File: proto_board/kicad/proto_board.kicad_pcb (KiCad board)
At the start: 2 copper layers, 80 x 50 mm, 1 part, among them J1 pcie_98

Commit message: Work in progress. Backlane kicad.
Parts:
- added H1: Bracket Hole, MountingHole:MountingHole_3.2mm_M3_Pad_Via, F.Cu at (95.5, 56.5)
- added H2: Bracket Hole, MountingHole:MountingHole_3.2mm_M3_Pad_Via, F.Cu at (95.4, 94.8)
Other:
- outline, holes or cut-outs redrawn

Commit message: Proto board work in progress.
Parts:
- removed H1, H2: Bracket Hole, MountingHole:MountingHole_3.2mm_M3_Pad_Via
- added J2: Conn_02x25_Odd_Even, Connector_PinHeader_2.00mm:PinHeader_2x25_P2.00mm_Vertical_SMD, F.Cu at (126.0, 96.1)
- added J3: Conn_02x25_Odd_Even, Connector_PinHeader_2.00mm:PinHeader_2x25_P2.00mm_Vertical_SMD, F.Cu at (126.0, 87.1)
- added TP1: TestPoint, proto_board:pad, F.Cu at (147.3, 55.9)
- added TP1: TestPoint, proto_board:pad, F.Cu at (144.8, 55.9)
- added TP1: TestPoint, proto_board:pad, F.Cu at (162.6, 86.4)
- added TP1: TestPoint, proto_board:pad, F.Cu at (149.9, 78.7)
- added TP1: TestPoint, proto_board:pad, F.Cu at (94.0, 58.4)
- added TP1: TestPoint, proto_board:pad, F.Cu at (129.5, 53.3)
- added TP1: TestPoint, proto_board:pad, F.Cu at (175.3, 86.4)
- added TP1: TestPoint, proto_board:pad, F.Cu at (157.5, 83.8)
- added TP1: TestPoint, proto_board:pad, F.Cu at (177.8, 43.2)
- added TP1: TestPoint, proto_board:pad, F.Cu at (170.2, 78.7)
- added TP1: TestPoint, proto_board:pad, F.Cu at (144.8, 81.3)
- added TP1: TestPoint, proto_board:pad, F.Cu at (142.2, 50.8)
- added TP1: TestPoint, proto_board:pad, F.Cu at (190.5, 43.2)
- added TP1: TestPoint, proto_board:pad, F.Cu at (127.0, 43.2)
- added TP1: TestPoint, proto_board:pad, F.Cu at (134.6, 50.8)
- added TP1: TestPoint, proto_board:pad, F.Cu at (114.3, 73.7)
- added TP1: TestPoint, proto_board:pad, F.Cu at (167.6, 66.0)
- added TP1: TestPoint, proto_board:pad, F.Cu at (180.3, 53.3)
- added TP1: TestPoint, proto_board:pad, F.Cu at (94.0, 76.2)
- added TP1: TestPoint, proto_board:pad, F.Cu at (175.3, 81.3)
- added TP1: TestPoint, proto_board:pad, F.Cu at (165.1, 91.4)
- added TP1: TestPoint, proto_board:pad, F.Cu at (101.6, 71.1)
- added TP1: TestPoint, proto_board:pad, F.Cu at (185.4, 81.3)
- added TP1: TestPoint, proto_board:pad, F.Cu at (101.6, 73.7)
- added TP1: TestPoint, proto_board:pad, F.Cu at (188.0, 81.3)
- added TP1: TestPoint, proto_board:pad, F.Cu at (180.3, 83.8)
- added TP1: TestPoint, proto_board:pad, F.Cu at (165.1, 81.3)
- added TP1: TestPoint, proto_board:pad, F.Cu at (188.0, 73.7)
- added TP1: TestPoint, proto_board:pad, F.Cu at (195.6, 83.8)
- added TP1: TestPoint, proto_board:pad, F.Cu at (111.8, 78.7)
- added TP1: TestPoint, proto_board:pad, F.Cu at (127.0, 73.7)
- added TP1: TestPoint, proto_board:pad, F.Cu at (139.7, 61.0)
- added TP1: TestPoint, proto_board:pad, F.Cu at (185.4, 61.0)
- added TP1: TestPoint, proto_board:pad, F.Cu at (180.3, 81.3)
- added TP1: TestPoint, proto_board:pad, F.Cu at (101.6, 76.2)
- added TP1: TestPoint, proto_board:pad, F.Cu at (170.2, 61.0)
- added TP1: TestPoint, proto_board:pad, F.Cu at (101.6, 43.2)
- added TP1: TestPoint, proto_board:pad, F.Cu at (144.8, 66.0)
- added TP1: TestPoint, proto_board:pad, F.Cu at (175.3, 45.7)
- added TP1: TestPoint, proto_board:pad, F.Cu at (96.5, 88.9)
- added TP1: TestPoint, proto_board:pad, F.Cu at (152.4, 68.6)
- added TP1: TestPoint, proto_board:pad, F.Cu at (180.3, 91.4)
- added TP1: TestPoint, proto_board:pad, F.Cu at (91.4, 68.6)
- added TP1: TestPoint, proto_board:pad, F.Cu at (134.6, 48.3)
- added TP1: TestPoint, proto_board:pad, F.Cu at (170.2, 68.6)
- added TP1: TestPoint, proto_board:pad, F.Cu at (142.2, 55.9)
- added TP1: TestPoint, proto_board:pad, F.Cu at (167.6, 96.5)
- added TP1: TestPoint, proto_board:pad, F.Cu at (94.0, 63.5)
- added TP1: TestPoint, proto_board:pad, F.Cu at (96.5, 53.3)
- added TP1: TestPoint, proto_board:pad, F.Cu at (144.8, 48.3)
- added TP1: TestPoint, proto_board:pad, F.Cu at (124.5, 50.8)
- added TP1: TestPoint, proto_board:pad, F.Cu at (111.8, 43.2)
- added TP1: TestPoint, proto_board:pad, F.Cu at (91.4, 61.0)
- added TP1: TestPoint, proto_board:pad, F.Cu at (149.9, 48.3)
- added TP1: TestPoint, proto_board:pad, F.Cu at (106.7, 50.8)
- added TP1: TestPoint, proto_board:pad, F.Cu at (132.1, 76.2)
- added TP1: TestPoint, proto_board:pad, F.Cu at (114.3, 71.1)
- added TP1: TestPoint, proto_board:pad, F.Cu at (177.8, 76.2)
- added TP1: TestPoint, proto_board:pad, F.Cu at (94.0, 68.6)
- added TP1: TestPoint, proto_board:pad, F.Cu at (137.2, 66.0)
- added TP1: TestPoint, proto_board:pad, F.Cu at (195.6, 86.4)
- added TP1: TestPoint, proto_board:pad, F.Cu at (185.4, 78.7)
- added TP1: TestPoint, proto_board:pad, F.Cu at (152.4, 55.9)
- added TP1: TestPoint, proto_board:pad, F.Cu at (193.0, 48.3)
- added TP1: TestPoint, proto_board:pad, F.Cu at (198.1, 73.7)
- added TP1: TestPoint, proto_board:pad, F.Cu at (160.0, 96.5)
- added TP1: TestPoint, proto_board:pad, F.Cu at (129.5, 68.6)
- added TP1: TestPoint, proto_board:pad, F.Cu at (180.3, 58.4)
- added TP1: TestPoint, proto_board:pad, F.Cu at (190.5, 96.5)
- added TP1: TestPoint, proto_board:pad, F.Cu at (121.9, 50.8)
- added TP1: TestPoint, proto_board:pad, F.Cu at (142.2, 43.2)
- added TP1: TestPoint, proto_board:pad, F.Cu at (132.1, 50.8)
- added TP1: TestPoint, proto_board:pad, F.Cu at (182.9, 58.4)
- added TP1: TestPoint, proto_board:pad, F.Cu at (195.6, 96.5)
- added TP1: TestPoint, proto_board:pad, F.Cu at (177.8, 58.4)
- added TP1: TestPoint, proto_board:pad, F.Cu at (99.1, 73.7)
- added TP1: TestPoint, proto_board:pad, F.Cu at (167.6, 45.7)
- added TP1: TestPoint, proto_board:pad, F.Cu at (190.5, 55.9)
- added TP1: TestPoint, proto_board:pad, F.Cu at (137.2, 71.1)
- added TP1: TestPoint, proto_board:pad, F.Cu at (147.3, 58.4)
- added TP1: TestPoint, proto_board:pad, F.Cu at (177.8, 83.8)
- added TP1: TestPoint, proto_board:pad, F.Cu at (139.7, 55.9)
- added TP1: TestPoint, proto_board:pad, F.Cu at (165.1, 66.0)
- added TP1: TestPoint, proto_board:pad, F.Cu at (154.9, 96.5)
- added TP1: TestPoint, proto_board:pad, F.Cu at (172.7, 94.0)
- added TP1: TestPoint, proto_board:pad, F.Cu at (152.4, 50.8)
- added TP1: TestPoint, proto_board:pad, F.Cu at (127.0, 53.3)
- added TP1: TestPoint, proto_board:pad, F.Cu at (139.7, 76.2)
- added TP1: TestPoint, proto_board:pad, F.Cu at (96.5, 50.8)
- added TP1: TestPoint, proto_board:pad, F.Cu at (195.6, 94.0)
- added TP1: TestPoint, proto_board:pad, F.Cu at (106.7, 66.0)
- added TP1: TestPoint, proto_board:pad, F.Cu at (198.1, 63.5)
- added TP1: TestPoint, proto_board:pad, F.Cu at (99.1, 58.4)
- added TP1: TestPoint, proto_board:pad, F.Cu at (99.1, 76.2)
- added TP1: TestPoint, proto_board:pad, F.Cu at (106.7, 61.0)
- added TP1: TestPoint, proto_board:pad, F.Cu at (167.6, 76.2)
- added TP1: TestPoint, proto_board:pad, F.Cu at (91.4, 50.8)
- added TP1: TestPoint, proto_board:pad, F.Cu at (185.4, 71.1)
- added TP1: TestPoint, proto_board:pad, F.Cu at (193.0, 96.5)
- added TP1: TestPoint, proto_board:pad, F.Cu at (193.0, 94.0)
- added TP1: TestPoint, proto_board:pad, F.Cu at (129.5, 61.0)
- added TP1: TestPoint, proto_board:pad, F.Cu at (124.5, 71.1)
- added TP1: TestPoint, proto_board:pad, F.Cu at (129.5, 58.4)
- added TP1: TestPoint, proto_board:pad, F.Cu at (144.8, 76.2)
- added TP1: TestPoint, proto_board:pad, F.Cu at (96.5, 58.4)
- added TP1: TestPoint, proto_board:pad, F.Cu at (188.0, 45.7)
- added TP1: TestPoint, proto_board:pad, F.Cu at (139.7, 50.8)
- added TP1: TestPoint, proto_board:pad, F.Cu at (114.3, 61.0)
- added TP1: TestPoint, proto_board:pad, F.Cu at (188.0, 96.5)
- added TP1: TestPoint, proto_board:pad, F.Cu at (198.1, 43.2)
- added TP1: TestPoint, proto_board:pad, F.Cu at (185.4, 53.3)
- added TP1: TestPoint, proto_board:pad, F.Cu at (96.5, 63.5)
- added TP1: TestPoint, proto_board:pad, F.Cu at (195.6, 68.6)
- added TP1: TestPoint, proto_board:pad, F.Cu at (182.9, 96.5)
- added TP1: TestPoint, proto_board:pad, F.Cu at (180.3, 61.0)
- added TP1: TestPoint, proto_board:pad, F.Cu at (129.5, 48.3)
- added TP1: TestPoint, proto_board:pad, F.Cu at (160.0, 94.0)
- added TP1: TestPoint, proto_board:pad, F.Cu at (188.0, 68.6)
- added TP1: TestPoint, proto_board:pad, F.Cu at (170.2, 55.9)
- added TP1: TestPoint, proto_board:pad, F.Cu at (185.4, 91.4)
- added TP1: TestPoint, proto_board:pad, F.Cu at (180.3, 86.4)
- added TP1: TestPoint, proto_board:pad, F.Cu at (160.0, 61.0)
- added TP1: TestPoint, proto_board:pad, F.Cu at (185.4, 63.5)
- added TP1: TestPoint, proto_board:pad, F.Cu at (195.6, 55.9)
- added TP1: TestPoint, proto_board:pad, F.Cu at (182.9, 83.8)
- added TP1: TestPoint, proto_board:pad, F.Cu at (162.6, 76.2)
- added TP1: TestPoint, proto_board:pad, F.Cu at (154.9, 91.4)
- added TP1: TestPoint, proto_board:pad, F.Cu at (154.9, 45.7)
- added TP1: TestPoint, proto_board:pad, F.Cu at (162.6, 58.4)
- added TP1: TestPoint, proto_board:pad, F.Cu at (147.3, 53.3)
- added TP1: TestPoint, proto_board:pad, F.Cu at (124.5, 66.0)
- added TP1: TestPoint, proto_board:pad, F.Cu at (149.9, 76.2)
- added TP1: TestPoint, proto_board:pad, F.Cu at (170.2, 96.5)
- added TP1: TestPoint, proto_board:pad, F.Cu at (172.7, 50.8)
- added TP1: TestPoint, proto_board:pad, F.Cu at (94.0, 48.3)
- added TP1: TestPoint, proto_board:pad, F.Cu at (177.8, 86.4)
- added TP1: TestPoint, proto_board:pad, F.Cu at (149.9, 66.0)
- added TP1: TestPoint, proto_board:pad, F.Cu at (127.0, 58.4)
- added TP1: TestPoint, proto_board:pad, F.Cu at (119.4, 50.8)
- added TP1: TestPoint, proto_board:pad, F.Cu at (124.5, 45.7)
- added TP1: TestPoint, proto_board:pad, F.Cu at (190.5, 68.6)
- added TP1: TestPoint, proto_board:pad, F.Cu at (137.2, 73.7)
- added TP1: TestPoint, proto_board:pad, F.Cu at (193.0, 86.4)
- added TP1: TestPoint, proto_board:pad, F.Cu at (157.5, 53.3)
- added TP1: TestPoint, proto_board:pad, F.Cu at (165.1, 68.6)
- added TP1: TestPoint, proto_board:pad, F.Cu at (167.6, 81.3)
- added TP1: TestPoint, proto_board:pad, F.Cu at (198.1, 91.4)
- added TP1: TestPoint, proto_board:pad, F.Cu at (162.6, 50.8)
- added TP1: TestPoint, proto_board:pad, F.Cu at (147.3, 63.5)
- added TP1: TestPoint, proto_board:pad, F.Cu at (198.1, 88.9)
- added TP1: TestPoint, proto_board:pad, F.Cu at (154.9, 73.7)
- added TP1: TestPoint, proto_board:pad, F.Cu at (182.9, 55.9)
- added TP1: TestPoint, proto_board:pad, F.Cu at (162.6, 91.4)
- added TP1: TestPoint, proto_board:pad, F.Cu at (109.2, 71.1)
- added TP1: TestPoint, proto_board:pad, F.Cu at (167.6, 94.0)
- added TP1: TestPoint, proto_board:pad, F.Cu at (188.0, 66.0)
- added TP1: TestPoint, proto_board:pad, F.Cu at (129.5, 81.3)
- added TP1: TestPoint, proto_board:pad, F.Cu at (109.2, 50.8)
- added TP1: TestPoint, proto_board:pad, F.Cu at (198.1, 61.0)
- added TP1: TestPoint, proto_board:pad, F.Cu at (182.9, 78.7)
- added TP1: TestPoint, proto_board:pad, F.Cu at (144.8, 50.8)
- added TP1: TestPoint, proto_board:pad, F.Cu at (147.3, 50.8)
- added TP1: TestPoint, proto_board:pad, F.Cu at (104.1, 68.6)
- added TP1: TestPoint, proto_board:pad, F.Cu at (195.6, 53.3)
- added TP1: TestPoint, proto_board:pad, F.Cu at (101.6, 63.5)
- added TP1: TestPoint, proto_board:pad, F.Cu at (111.8, 48.3)
- added TP1: TestPoint, proto_board:pad, F.Cu at (167.6, 63.5)
- added TP1: TestPoint, proto_board:pad, F.Cu at (142.2, 53.3)
- added TP1: TestPoint, proto_board:pad, F.Cu at (134.6, 45.7)
- added TP1: TestPoint, proto_board:pad, F.Cu at (109.2, 63.5)
- added TP1: TestPoint, proto_board:pad, F.Cu at (124.5, 81.3)
- added TP1: TestPoint, proto_board:pad, F.Cu at (162.6, 81.3)
- added TP1: TestPoint, proto_board:pad, F.Cu at (134.6, 81.3)
- added TP1: TestPoint, proto_board:pad, F.Cu at (137.2, 58.4)
- added TP1: TestPoint, proto_board:pad, F.Cu at (154.9, 88.9)
- added TP1: TestPoint, proto_board:pad, F.Cu at (152.4, 48.3)
- added TP1: TestPoint, proto_board:pad, F.Cu at (172.7, 96.5)
- added TP1: TestPoint, proto_board:pad, F.Cu at (94.0, 83.8)
- added TP1: TestPoint, proto_board:pad, F.Cu at (175.3, 55.9)
- added TP1: TestPoint, proto_board:pad, F.Cu at (119.4, 55.9)
- added TP1: TestPoint, proto_board:pad, F.Cu at (162.6, 66.0)
- added TP1: TestPoint, proto_board:pad, F.Cu at (142.2, 73.7)
- added TP1: TestPoint, proto_board:pad, F.Cu at (198.1, 96.5)
- added TP1: TestPoint, proto_board:pad, F.Cu at (152.4, 45.7)
- added TP1: TestPoint, proto_board:pad, F.Cu at (121.9, 55.9)
- added TP1: TestPoint, proto_board:pad, F.Cu at (195.6, 63.5)
- added TP1: TestPoint, proto_board:pad, F.Cu at (111.8, 71.1)
- added TP1: TestPoint, proto_board:pad, F.Cu at (157.5, 94.0)
- added TP1: TestPoint, proto_board:pad, F.Cu at (188.0, 71.1)
- added TP1: TestPoint, proto_board:pad, F.Cu at (170.2, 88.9)
- added TP1: TestPoint, proto_board:pad, F.Cu at (119.4, 43.2)
- added TP1: TestPoint, proto_board:pad, F.Cu at (111.8, 61.0)
- added TP1: TestPoint, proto_board:pad, F.Cu at (147.3, 78.7)
- added TP1: TestPoint, proto_board:pad, F.Cu at (154.9, 66.0)
- added TP1: TestPoint, proto_board:pad, F.Cu at (106.7, 78.7)
- added TP1: TestPoint, proto_board:pad, F.Cu at (172.7, 53.3)
- added TP1: TestPoint, proto_board:pad, F.Cu at (182.9, 76.2)
- added TP1: TestPoint, proto_board:pad, F.Cu at (147.3, 71.1)
- added TP1: TestPoint, proto_board:pad, F.Cu at (157.5, 76.2)
- added TP1: TestPoint, proto_board:pad, F.Cu at (109.2, 66.0)
- added TP1: TestPoint, proto_board:pad, F.Cu at (114.3, 58.4)
- added TP1: TestPoint, proto_board:pad, F.Cu at (185.4, 66.0)
- added TP1: TestPoint, proto_board:pad, F.Cu at (195.6, 66.0)
- added TP1: TestPoint, proto_board:pad, F.Cu at (99.1, 68.6)
- added TP1: TestPoint, proto_board:pad, F.Cu at (127.0, 55.9)
- added TP1: TestPoint, proto_board:pad, F.Cu at (121.9, 63.5)
- added TP1: TestPoint, proto_board:pad, F.Cu at (121.9, 78.7)
- added TP1: TestPoint, proto_board:pad, F.Cu at (144.8, 43.2)
- added TP1: TestPoint, proto_board:pad, F.Cu at (116.8, 78.7)
- added TP1: TestPoint, proto_board:pad, F.Cu at (119.4, 53.3)
- added TP1: TestPoint, proto_board:pad, F.Cu at (124.5, 58.4)
- added TP1: TestPoint, proto_board:pad, F.Cu at (149.9, 81.3)
- added TP1: TestPoint, proto_board:pad, F.Cu at (190.5, 88.9)
- added TP1: TestPoint, proto_board:pad, F.Cu at (175.3, 88.9)
- added TP1: TestPoint, proto_board:pad, F.Cu at (182.9, 50.8)
- added TP1: TestPoint, proto_board:pad, F.Cu at (111.8, 76.2)
- added TP1: TestPoint, proto_board:pad, F.Cu at (165.1, 73.7)
- added TP1: TestPoint, proto_board:pad, F.Cu at (96.5, 76.2)
- added TP1: TestPoint, proto_board:pad, F.Cu at (162.6, 78.7)
- added TP1: TestPoint, proto_board:pad, F.Cu at (147.3, 73.7)
- added TP1: TestPoint, proto_board:pad, F.Cu at (170.2, 86.4)
- added TP1: TestPoint, proto_board:pad, F.Cu at (121.9, 76.2)
- added TP1: TestPoint, proto_board:pad, F.Cu at (193.0, 81.3)
- added TP1: TestPoint, proto_board:pad, F.Cu at (142.2, 78.7)
- added TP1: TestPoint, proto_board:pad, F.Cu at (182.9, 94.0)
- added TP1: TestPoint, proto_board:pad, F.Cu at (91.4, 76.2)
- added TP1: TestPoint, proto_board:pad, F.Cu at (139.7, 53.3)
- added TP1: TestPoint, proto_board:pad, F.Cu at (188.0, 55.9)
- added TP1: TestPoint, proto_board:pad, F.Cu at (175.3, 76.2)
- added TP1: TestPoint, proto_board:pad, F.Cu at (193.0, 91.4)
- added TP1: TestPoint, proto_board:pad, F.Cu at (106.7, 45.7)
- added TP1: TestPoint, proto_board:pad, F.Cu at (170.2, 76.2)
- added TP1: TestPoint, proto_board:pad, F.Cu at (127.0, 81.3)
- added TP1: TestPoint, proto_board:pad, F.Cu at (188.0, 61.0)
- added TP1: TestPoint, proto_board:pad, F.Cu at (160.0, 76.2)
- added TP1: TestPoint, proto_board:pad, F.Cu at (109.2, 55.9)
- added TP1: TestPoint, proto_board:pad, F.Cu at (94.0, 50.8)
- added TP1: TestPoint, proto_board:pad, F.Cu at (111.8, 81.3)
- added TP1: TestPoint, proto_board:pad, F.Cu at (190.5, 58.4)
- added TP1: TestPoint, proto_board:pad, F.Cu at (116.8, 48.3)
- added TP1: TestPoint, proto_board:pad, F.Cu at (109.2, 48.3)
- added TP1: TestPoint, proto_board:pad, F.Cu at (152.4, 81.3)
- added TP1: TestPoint, proto_board:pad, F.Cu at (157.5, 73.7)
- added TP1: TestPoint, proto_board:pad, F.Cu at (195.6, 48.3)
- added TP1: TestPoint, proto_board:pad, F.Cu at (170.2, 58.4)
- added TP1: TestPoint, proto_board:pad, F.Cu at (165.1, 45.7)
- added TP1: TestPoint, proto_board:pad, F.Cu at (177.8, 45.7)
- added TP1: TestPoint, proto_board:pad, F.Cu at (137.2, 68.6)
- added TP1: TestPoint, proto_board:pad, F.Cu at (127.0, 78.7)
- added TP1: TestPoint, proto_board:pad, F.Cu at (129.5, 71.1)
- added TP1: TestPoint, proto_board:pad, F.Cu at (198.1, 81.3)
- added TP1: TestPoint, proto_board:pad, F.Cu at (175.3, 58.4)
- added TP1: TestPoint, proto_board:pad, F.Cu at (182.9, 81.3)
- added TP1: TestPoint, proto_board:pad, F.Cu at (170.2, 83.8)
- added TP1: TestPoint, proto_board:pad, F.Cu at (129.5, 55.9)
- added TP1: TestPoint, proto_board:pad, F.Cu at (165.1, 61.0)
- added TP1: TestPoint, proto_board:pad, F.Cu at (124.5, 43.2)
- added TP1: TestPoint, proto_board:pad, F.Cu at (139.7, 78.7)
- added TP1: TestPoint, proto_board:pad, F.Cu at (172.7, 68.6)
- added TP1: TestPoint, proto_board:pad, F.Cu at (172.7, 76.2)
- added TP1: TestPoint, proto_board:pad, F.Cu at (132.1, 48.3)
- added TP1: TestPoint, proto_board:pad, F.Cu at (127.0, 48.3)
- added TP1: TestPoint, proto_board:pad, F.Cu at (132.1, 66.0)
- added TP1: TestPoint, proto_board:pad, F.Cu at (157.5, 86.4)
- added TP1: TestPoint, proto_board:pad, F.Cu at (157.5, 48.3)
- added TP1: TestPoint, proto_board:pad, F.Cu at (175.3, 43.2)
- added TP1: TestPoint, proto_board:pad, F.Cu at (185.4, 50.8)
- added TP1: TestPoint, proto_board:pad, F.Cu at (96.5, 73.7)
- added TP1: TestPoint, proto_board:pad, F.Cu at (147.3, 61.0)
- added TP1: TestPoint, proto_board:pad, F.Cu at (116.8, 50.8)
- added TP1: TestPoint, proto_board:pad, F.Cu at (154.9, 53.3)
- added TP1: TestPoint, proto_board:pad, F.Cu at (154.9, 94.0)
- added TP1: TestPoint, proto_board:pad, F.Cu at (157.5, 55.9)
- added TP1: TestPoint, proto_board:pad, F.Cu at (116.8, 76.2)
- added TP1: TestPoint, proto_board:pad, F.Cu at (139.7, 66.0)
- added TP1: TestPoint, proto_board:pad, F.Cu at (142.2, 45.7)
- added TP1: TestPoint, proto_board:pad, F.Cu at (182.9, 43.2)
- added TP1: TestPoint, proto_board:pad, F.Cu at (96.5, 83.8)
- added TP1: TestPoint, proto_board:pad, F.Cu at (119.4, 81.3)
- added TP1: TestPoint, proto_board:pad, F.Cu at (94.0, 66.0)
- added TP1: TestPoint, proto_board:pad, F.Cu at (188.0, 63.5)
- added TP1: TestPoint, proto_board:pad, F.Cu at (111.8, 68.6)
- added TP1: TestPoint, proto_board:pad, F.Cu at (157.5, 91.4)
- added TP1: TestPoint, proto_board:pad, F.Cu at (175.3, 53.3)
- added TP1: TestPoint, proto_board:pad, F.Cu at (106.7, 53.3)
- added TP1: TestPoint, proto_board:pad, F.Cu at (119.4, 68.6)
- added TP1: TestPoint, proto_board:pad, F.Cu at (180.3, 88.9)
- added TP1: TestPoint, proto_board:pad, F.Cu at (142.2, 58.4)
- added TP1: TestPoint, proto_board:pad, F.Cu at (94.0, 78.7)
- added TP1: TestPoint, proto_board:pad, F.Cu at (157.5, 58.4)
- added TP1: TestPoint, proto_board:pad, F.Cu at (139.7, 43.2)
- added TP1: TestPoint, proto_board:pad, F.Cu at (182.9, 45.7)
- added TP1: TestPoint, proto_board:pad, F.Cu at (177.8, 91.4)
- added TP1: TestPoint, proto_board:pad, F.Cu at (152.4, 76.2)
- added TP1: TestPoint, proto_board:pad, F.Cu at (96.5, 61.0)
- added TP1: TestPoint, proto_board:pad, F.Cu at (180.3, 63.5)
- added TP1: TestPoint, proto_board:pad, F.Cu at (149.9, 61.0)
- added TP1: TestPoint, proto_board:pad, F.Cu at (195.6, 81.3)
- added TP1: TestPoint, proto_board:pad, F.Cu at (106.7, 63.5)
- added TP1: TestPoint, proto_board:pad, F.Cu at (137.2, 48.3)
- added TP1: TestPoint, proto_board:pad, F.Cu at (165.1, 76.2)
- added TP1: TestPoint, proto_board:pad, F.Cu at (91.4, 55.9)
- added TP1: TestPoint, proto_board:pad, F.Cu at (157.5, 71.1)
- added TP1: TestPoint, proto_board:pad, F.Cu at (137.2, 61.0)
- added TP1: TestPoint, proto_board:pad, F.Cu at (193.0, 53.3)
- added TP1: TestPoint, proto_board:pad, F.Cu at (190.5, 71.1)
- added TP1: TestPoint, proto_board:pad, F.Cu at (172.7, 61.0)
- added TP1: TestPoint, proto_board:pad, F.Cu at (157.5, 68.6)
- added TP1: TestPoint, proto_board:pad, F.Cu at (127.0, 63.5)
- added TP1: TestPoint, proto_board:pad, F.Cu at (119.4, 73.7)
- added TP1: TestPoint, proto_board:pad, F.Cu at (160.0, 68.6)
- added TP1: TestPoint, proto_board:pad, F.Cu at (160.0, 81.3)
- added TP1: TestPoint, proto_board:pad, F.Cu at (172.7, 43.2)
- added TP1: TestPoint, proto_board:pad, F.Cu at (94.0, 96.5)
- added TP1: TestPoint, proto_board:pad, F.Cu at (104.1, 45.7)
- added TP1: TestPoint, proto_board:pad, F.Cu at (152.4, 43.2)
- added TP1: TestPoint, proto_board:pad, F.Cu at (170.2, 43.2)
- added TP1: TestPoint, proto_board:pad, F.Cu at (190.5, 94.0)
- added TP1: TestPoint, proto_board:pad, F.Cu at (198.1, 68.6)
- added TP1: TestPoint, proto_board:pad, F.Cu at (195.6, 88.9)
- added TP1: TestPoint, proto_board:pad, F.Cu at (154.9, 81.3)
- added TP1: TestPoint, proto_board:pad, F.Cu at (99.1, 66.0)
- added TP1: TestPoint, proto_board:pad, F.Cu at (144.8, 45.7)
- added TP1: TestPoint, proto_board:pad, F.Cu at (157.5, 96.5)
- added TP1: TestPoint, proto_board:pad, F.Cu at (124.5, 48.3)
- added TP1: TestPoint, proto_board:pad, F.Cu at (101.6, 81.3)
- added TP1: TestPoint, proto_board:pad, F.Cu at (175.3, 50.8)
- added TP1: TestPoint, proto_board:pad, F.Cu at (139.7, 58.4)
- added TP1: TestPoint, proto_board:pad, F.Cu at (160.0, 66.0)
- added TP1: TestPoint, proto_board:pad, F.Cu at (157.5, 88.9)
- added TP1: TestPoint, proto_board:pad, F.Cu at (154.9, 83.8)
- added TP1: TestPoint, proto_board:pad, F.Cu at (147.3, 43.2)
- added TP1: TestPoint, proto_board:pad, F.Cu at (101.6, 58.4)
- added TP1: TestPoint, proto_board:pad, F.Cu at (139.7, 71.1)
- added TP1: TestPoint, proto_board:pad, F.Cu at (172.7, 71.1)
- added TP1: TestPoint, proto_board:pad, F.Cu at (160.0, 91.4)
- added TP1: TestPoint, proto_board:pad, F.Cu at (172.7, 45.7)
- added TP1: TestPoint, proto_board:pad, F.Cu at (137.2, 81.3)
- added TP1: TestPoint, proto_board:pad, F.Cu at (188.0, 76.2)
- added TP1: TestPoint, proto_board:pad, F.Cu at (170.2, 66.0)
- added TP1: TestPoint, proto_board:pad, F.Cu at (190.5, 81.3)
- added TP1: TestPoint, proto_board:pad, F.Cu at (182.9, 48.3)
- added TP1: TestPoint, proto_board:pad, F.Cu at (185.4, 73.7)
- added TP1: TestPoint, proto_board:pad, F.Cu at (137.2, 53.3)
- added TP1: TestPoint, proto_board:pad, F.Cu at (160.0, 73.7)
- added TP1: TestPoint, proto_board:pad, F.Cu at (172.7, 55.9)
- added TP1: TestPoint, proto_board:pad, F.Cu at (162.6, 83.8)
- added TP1: TestPoint, proto_board:pad, F.Cu at (104.1, 50.8)
- added TP1: TestPoint, proto_board:pad, F.Cu at (172.7, 63.5)
- added TP1: TestPoint, proto_board:pad, F.Cu at (121.9, 68.6)
- added TP1: TestPoint, proto_board:pad, F.Cu at (193.0, 66.0)
- added TP1: TestPoint, proto_board:pad, F.Cu at (175.3, 73.7)
- added TP1: TestPoint, proto_board:pad, F.Cu at (96.5, 94.0)
- added TP1: TestPoint, proto_board:pad, F.Cu at (91.4, 58.4)
- added TP1: TestPoint, proto_board:pad, F.Cu at (185.4, 76.2)
- added TP1: TestPoint, proto_board:pad, F.Cu at (185.4, 68.6)
- added TP1: TestPoint, proto_board:pad, F.Cu at (193.0, 58.4)
- added TP1: TestPoint, proto_board:pad, F.Cu at (147.3, 68.6)
- added TP1: TestPoint, proto_board:pad, F.Cu at (96.5, 78.7)
- added TP1: TestPoint, proto_board:pad, F.Cu at (170.2, 91.4)
- added TP1: TestPoint, proto_board:pad, F.Cu at (134.6, 63.5)
- added TP1: TestPoint, proto_board:pad, F.Cu at (134.6, 55.9)
- added TP1: TestPoint, proto_board:pad, F.Cu at (99.1, 53.3)
- added TP1: TestPoint, proto_board:pad, F.Cu at (124.5, 53.3)
- added TP1: TestPoint, proto_board:pad, F.Cu at (104.1, 81.3)
- added TP1: TestPoint, proto_board:pad, F.Cu at (193.0, 55.9)
- added TP1: TestPoint, proto_board:pad, F.Cu at (91.4, 78.7)
- added TP1: TestPoint, proto_board:pad, F.Cu at (172.7, 73.7)
- added TP1: TestPoint, proto_board:pad, F.Cu at (152.4, 73.7)
- added TP1: TestPoint, proto_board:pad, F.Cu at (193.0, 50.8)
- added TP1: TestPoint, proto_board:pad, F.Cu at (190.5, 48.3)
- added TP1: TestPoint, proto_board:pad, F.Cu at (182.9, 63.5)
- added TP1: TestPoint, proto_board:pad, F.Cu at (142.2, 48.3)
- added TP1: TestPoint, proto_board:pad, F.Cu at (172.7, 88.9)
- added TP1: TestPoint, proto_board:pad, F.Cu at (121.9, 45.7)
- added TP1: TestPoint, proto_board:pad, F.Cu at (137.2, 78.7)
- added TP1: TestPoint, proto_board:pad, F.Cu at (185.4, 96.5)
- added TP1: TestPoint, proto_board:pad, F.Cu at (195.6, 45.7)
- added TP1: TestPoint, proto_board:pad, F.Cu at (109.2, 76.2)
- added TP1: TestPoint, proto_board:pad, F.Cu at (142.2, 68.6)
- added TP1: TestPoint, proto_board:pad, F.Cu at (119.4, 58.4)
- added TP1: TestPoint, proto_board:pad, F.Cu at (137.2, 45.7)
- added TP1: TestPoint, proto_board:pad, F.Cu at (170.2, 73.7)
- added TP1: TestPoint, proto_board:pad, F.Cu at (91.4, 63.5)
- added TP1: TestPoint, proto_board:pad, F.Cu at (111.8, 73.7)
- added TP1: TestPoint, proto_board:pad, F.Cu at (109.2, 53.3)
- added TP1: TestPoint, proto_board:pad, F.Cu at (129.5, 50.8)
- added TP1: TestPoint, proto_board:pad, F.Cu at (165.1, 58.4)
- added TP1: TestPoint, proto_board:pad, F.Cu at (132.1, 78.7)
- added TP1: TestPoint, proto_board:pad, F.Cu at (160.0, 78.7)
- added TP1: TestPoint, proto_board:pad, F.Cu at (121.9, 71.1)
- added TP1: TestPoint, proto_board:pad, F.Cu at (139.7, 68.6)
- added TP1: TestPoint, proto_board:pad, F.Cu at (91.4, 48.3)
- added TP1: TestPoint, proto_board:pad, F.Cu at (101.6, 68.6)
- added TP1: TestPoint, proto_board:pad, F.Cu at (165.1, 83.8)
- added TP1: TestPoint, proto_board:pad, F.Cu at (175.3, 66.0)
- added TP1: TestPoint, proto_board:pad, F.Cu at (154.9, 71.1)
- added TP1: TestPoint, proto_board:pad, F.Cu at (188.0, 86.4)
- added TP1: TestPoint, proto_board:pad, F.Cu at (104.1, 61.0)
- added TP1: TestPoint, proto_board:pad, F.Cu at (185.4, 55.9)
- added TP1: TestPoint, proto_board:pad, F.Cu at (132.1, 45.7)
- added TP1: TestPoint, proto_board:pad, F.Cu at (111.8, 66.0)
- added TP1: TestPoint, proto_board:pad, F.Cu at (119.4, 76.2)
- added TP1: TestPoint, proto_board:pad, F.Cu at (99.1, 43.2)
- added TP1: TestPoint, proto_board:pad, F.Cu at (94.0, 45.7)
- added TP1: TestPoint, proto_board:pad, F.Cu at (144.8, 68.6)
- added TP1: TestPoint, proto_board:pad, F.Cu at (114.3, 50.8)
- added TP1: TestPoint, proto_board:pad, F.Cu at (94.0, 86.4)
- added TP1: TestPoint, proto_board:pad, F.Cu at (190.5, 50.8)
- added TP1: TestPoint, proto_board:pad, F.Cu at (193.0, 61.0)
- added TP1: TestPoint, proto_board:pad, F.Cu at (104.1, 53.3)
- added TP1: TestPoint, proto_board:pad, F.Cu at (195.6, 61.0)
- added TP1: TestPoint, proto_board:pad, F.Cu at (109.2, 73.7)
- added TP1: TestPoint, proto_board:pad, F.Cu at (127.0, 45.7)
- added TP1: TestPoint, proto_board:pad, F.Cu at (91.4, 96.5)
- added TP1: TestPoint, proto_board:pad, F.Cu at (142.2, 61.0)
- added TP1: TestPoint, proto_board:pad, F.Cu at (99.1, 78.7)
- added TP1: TestPoint, proto_board:pad, F.Cu at (91.4, 71.1)
- added TP1: TestPoint, proto_board:pad, F.Cu at (154.9, 55.9)
- added TP1: TestPoint, proto_board:pad, F.Cu at (180.3, 76.2)
- added TP1: TestPoint, proto_board:pad, F.Cu at (124.5, 61.0)
- added TP1: TestPoint, proto_board:pad, F.Cu at (139.7, 63.5)
- added TP1: TestPoint, proto_board:pad, F.Cu at (175.3, 48.3)
- added TP1: TestPoint, proto_board:pad, F.Cu at (180.3, 55.9)
- added TP1: TestPoint, proto_board:pad, F.Cu at (190.5, 86.4)
- added TP1: TestPoint, proto_board:pad, F.Cu at (195.6, 43.2)
- added TP1: TestPoint, proto_board:pad, F.Cu at (124.5, 73.7)
- added TP1: TestPoint, proto_board:pad, F.Cu at (91.4, 45.7)
- added TP1: TestPoint, proto_board:pad, F.Cu at (142.2, 71.1)
- added TP1: TestPoint, proto_board:pad, F.Cu at (106.7, 81.3)
- added TP1: TestPoint, proto_board:pad, F.Cu at (180.3, 68.6)
- added TP1: TestPoint, proto_board:pad, F.Cu at (198.1, 48.3)
- added TP1: TestPoint, proto_board:pad, F.Cu at (180.3, 78.7)
- added TP1: TestPoint, proto_board:pad, F.Cu at (170.2, 81.3)
- added TP1: TestPoint, proto_board:pad, F.Cu at (190.5, 63.5)
- added TP1: TestPoint, proto_board:pad, F.Cu at (99.1, 61.0)
- added TP1: TestPoint, proto_board:pad, F.Cu at (96.5, 71.1)
- added TP1: TestPoint, proto_board:pad, F.Cu at (121.9, 43.2)
- added TP1: TestPoint, proto_board:pad, F.Cu at (188.0, 58.4)
- added TP1: TestPoint, proto_board:pad, F.Cu at (167.6, 58.4)
- added TP1: TestPoint, proto_board:pad, F.Cu at (147.3, 76.2)
- added TP1: TestPoint, proto_board:pad, F.Cu at (116.8, 73.7)
- added TP1: TestPoint, proto_board:pad, F.Cu at (96.5, 91.4)
- added TP1: TestPoint, proto_board:pad, F.Cu at (109.2, 68.6)
- added TP1: TestPoint, proto_board:pad, F.Cu at (175.3, 94.0)
- added TP1: TestPoint, proto_board:pad, F.Cu at (154.9, 86.4)
- added TP1: TestPoint, proto_board:pad, F.Cu at (144.8, 61.0)
- added TP1: TestPoint, proto_board:pad, F.Cu at (134.6, 53.3)
- added TP1: TestPoint, proto_board:pad, F.Cu at (170.2, 63.5)
- added TP1: TestPoint, proto_board:pad, F.Cu at (167.6, 68.6)
- added TP1: TestPoint, proto_board:pad, F.Cu at (193.0, 76.2)
- added TP1: TestPoint, proto_board:pad, F.Cu at (114.3, 81.3)
- added TP1: TestPoint, proto_board:pad, F.Cu at (116.8, 45.7)
- added TP1: TestPoint, proto_board:pad, F.Cu at (165.1, 88.9)
- added TP1: TestPoint, proto_board:pad, F.Cu at (116.8, 81.3)
- added TP1: TestPoint, proto_board:pad, F.Cu at (134.6, 71.1)
- added TP1: TestPoint, proto_board:pad, F.Cu at (195.6, 76.2)
- added TP1: TestPoint, proto_board:pad, F.Cu at (99.1, 48.3)
- added TP1: TestPoint, proto_board:pad, F.Cu at (149.9, 71.1)
- added TP1: TestPoint, proto_board:pad, F.Cu at (175.3, 68.6)
- added TP1: TestPoint, proto_board:pad, F.Cu at (190.5, 45.7)
- added TP1: TestPoint, proto_board:pad, F.Cu at (114.3, 76.2)
- added TP1: TestPoint, proto_board:pad, F.Cu at (193.0, 88.9)
- added TP1: TestPoint, proto_board:pad, F.Cu at (157.5, 78.7)
- added TP1: TestPoint, proto_board:pad, F.Cu at (162.6, 43.2)
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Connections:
- J1 pad A1: (no net) -> /A1
- J1 pad A10: (no net) -> unconnected-(J1-Pin_a10-PadA10)
- J1 pad A11: (no net) -> unconnected-(J1-Pin_A11-PadA11)
- J1 pad A12: (no net) -> unconnected-(J1-Pin_a12-PadA12)
- J1 pad A13: (no net) -> unconnected-(J1-Pin_a13-PadA13)
- J1 pad A14: (no net) -> unconnected-(J1-Pin_a14-PadA14)
- J1 pad A15: (no net) -> unconnected-(J1-Pin_a15-PadA15)
- J1 pad A16: (no net) -> unconnected-(J1-Pin_a16-PadA16)
- J1 pad A17: (no net) -> unconnected-(J1-Pin_a17-PadA17)
- J1 pad A18: (no net) -> unconnected-(J1-Pin_a18-PadA18)
- J1 pad A19: (no net) -> unconnected-(J1-Pin_a19-PadA19)
- J1 pad A2: (no net) -> /A2
- J1 pad A20: (no net) -> unconnected-(J1-Pin_a20-PadA20)
- J1 pad A21: (no net) -> unconnected-(J1-Pin_a21-PadA21)
- J1 pad A22: (no net) -> unconnected-(J1-Pin_a22-PadA22)
- J1 pad A23: (no net) -> unconnected-(J1-Pin_a23-PadA23)
- J1 pad A24: (no net) -> unconnected-(J1-Pin_a24-PadA24)
- J1 pad A25: (no net) -> unconnected-(J1-Pin_a25-PadA25)
- J1 pad A26: (no net) -> unconnected-(J1-Pin_a26-PadA26)
- J1 pad A27: (no net) -> unconnected-(J1-Pin_a27-PadA27)
- J1 pad A28: (no net) -> unconnected-(J1-Pin_a28-PadA28)
- J1 pad A29: (no net) -> unconnected-(J1-Pin_a29-PadA29)
- J1 pad A3: (no net) -> /A3
- J1 pad A30: (no net) -> unconnected-(J1-Pin_a30-PadA30)
- J1 pad A31: (no net) -> unconnected-(J1-Pin_a31-PadA31)
- J1 pad A32: (no net) -> unconnected-(J1-Pin_a32-PadA32)
- J1 pad A33: (no net) -> unconnected-(J1-Pin_a33-PadA33)
- J1 pad A34: (no net) -> unconnected-(J1-Pin_a34-PadA34)
- J1 pad A35: (no net) -> unconnected-(J1-Pin_a35-PadA35)
- J1 pad A36: (no net) -> unconnected-(J1-Pin_a36-PadA36)
- J1 pad A37: (no net) -> unconnected-(J1-Pin_a37-PadA37)
- J1 pad A38: (no net) -> unconnected-(J1-Pin_a38-PadA38)
- J1 pad A39: (no net) -> unconnected-(J1-Pin_a39-PadA39)
- J1 pad A4: (no net) -> /A4
- J1 pad A40: (no net) -> unconnected-(J1-Pin_a40-PadA40)
- J1 pad A41: (no net) -> unconnected-(J1-Pin_a41-PadA41)
- J1 pad A42: (no net) -> unconnected-(J1-Pin_a42-PadA42)
- J1 pad A43: (no net) -> unconnected-(J1-Pin_a43-PadA43)
- J1 pad A44: (no net) -> unconnected-(J1-Pin_a44-PadA44)
- J1 pad A45: (no net) -> unconnected-(J1-Pin_a45-PadA45)
- J1 pad A46: (no net) -> unconnected-(J1-Pin_a46-PadA46)
- J1 pad A47: (no net) -> unconnected-(J1-Pin_a47-PadA47)
- J1 pad A48: (no net) -> unconnected-(J1-Pin_a48-PadA48)
- J1 pad A49: (no net) -> unconnected-(J1-Pin_a49-PadA49)
- J1 pad A5: (no net) -> unconnected-(J1-Pin_a5-PadA5)
- J1 pad A6: (no net) -> unconnected-(J1-Pin_a6-PadA6)
- J1 pad A7: (no net) -> unconnected-(J1-Pin_a7-PadA7)
- J1 pad A8: (no net) -> unconnected-(J1-Pin_a8-PadA8)
- J1 pad A9: (no net) -> unconnected-(J1-Pin_a9-PadA9)
- J1 pad B1: (no net) -> /B1
- J1 pad B10: (no net) -> unconnected-(J1-Pin_b10-PadB10)
- J1 pad B11: (no net) -> unconnected-(J1-Pin_b11-PadB11)
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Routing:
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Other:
- board size 80 x 50 mm -> 113.1 x 62.3 mm
- board text added: "Conn_02x25_Odd_Even"

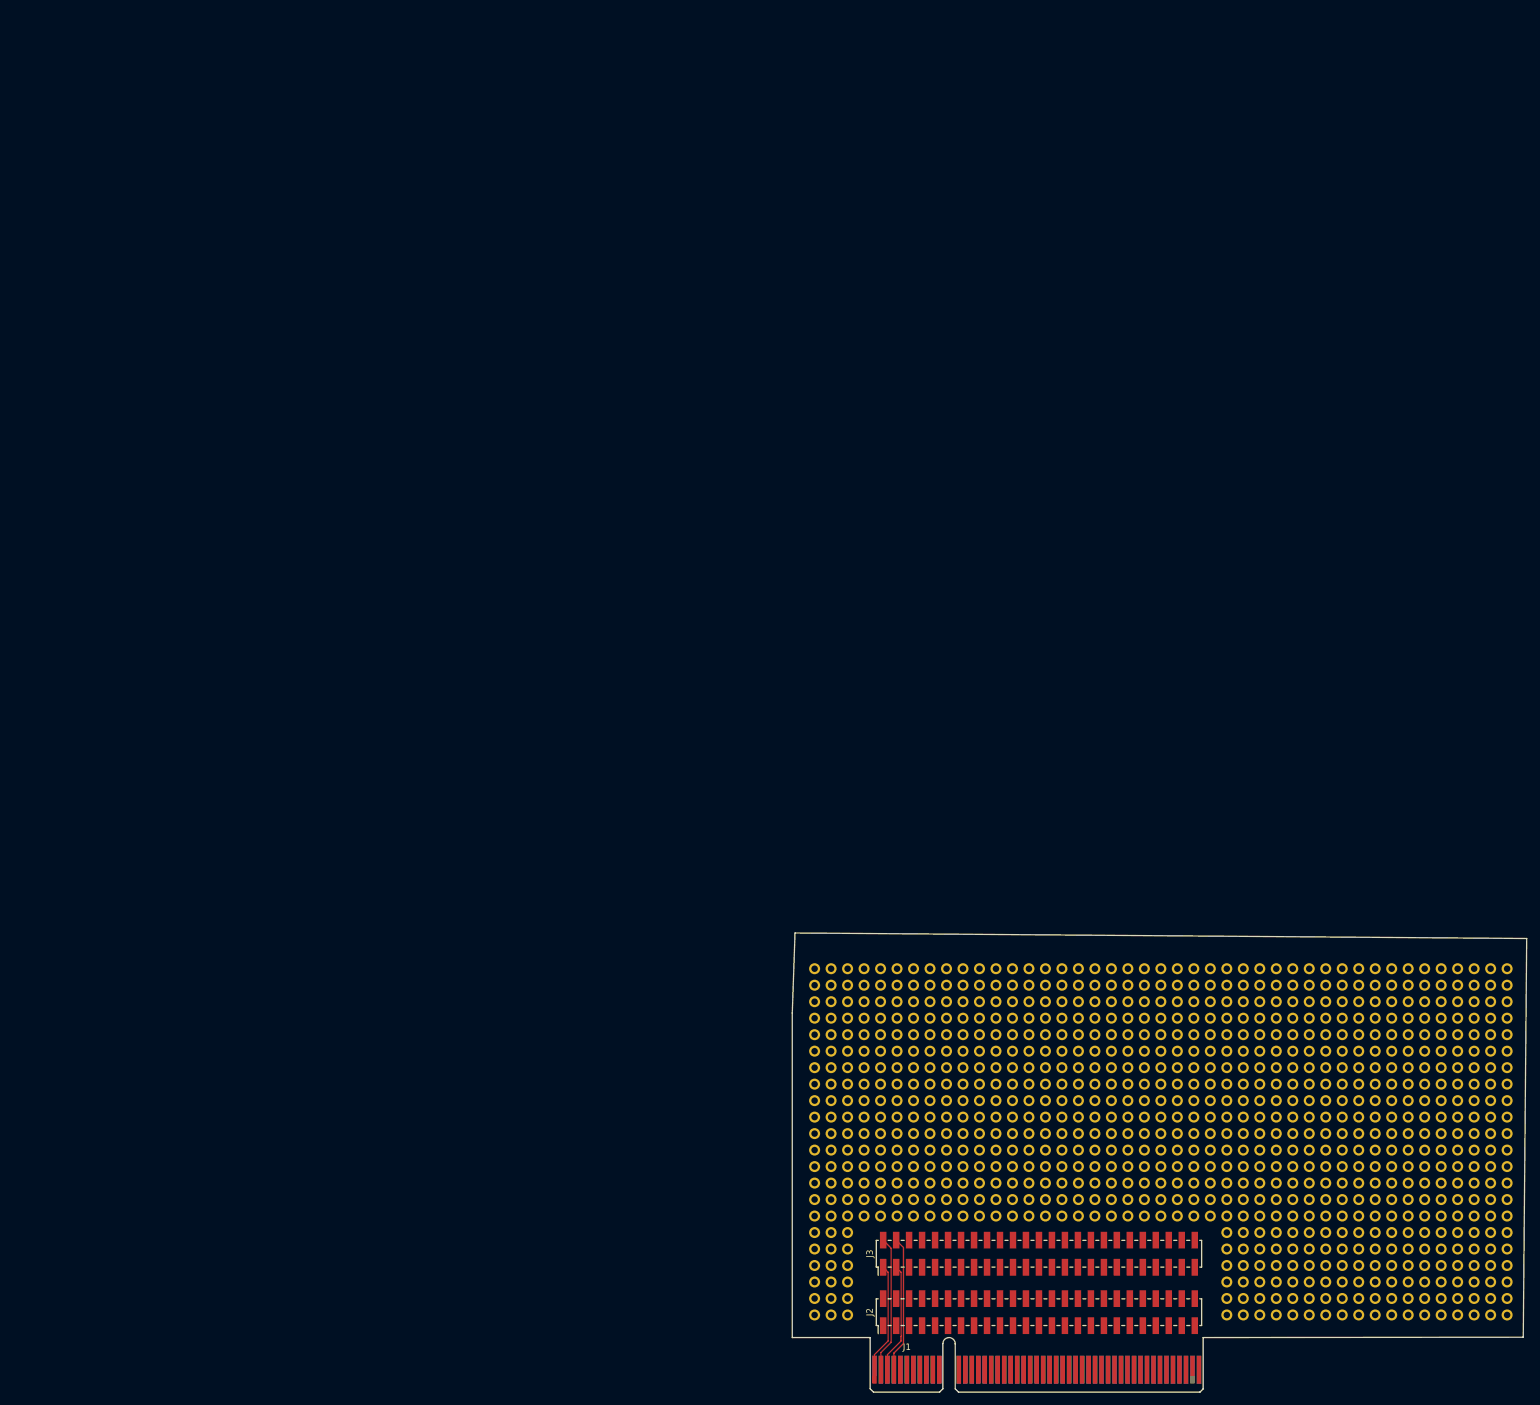
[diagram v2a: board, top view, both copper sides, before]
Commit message: Cleaned up the outline and fanout of the proto board.
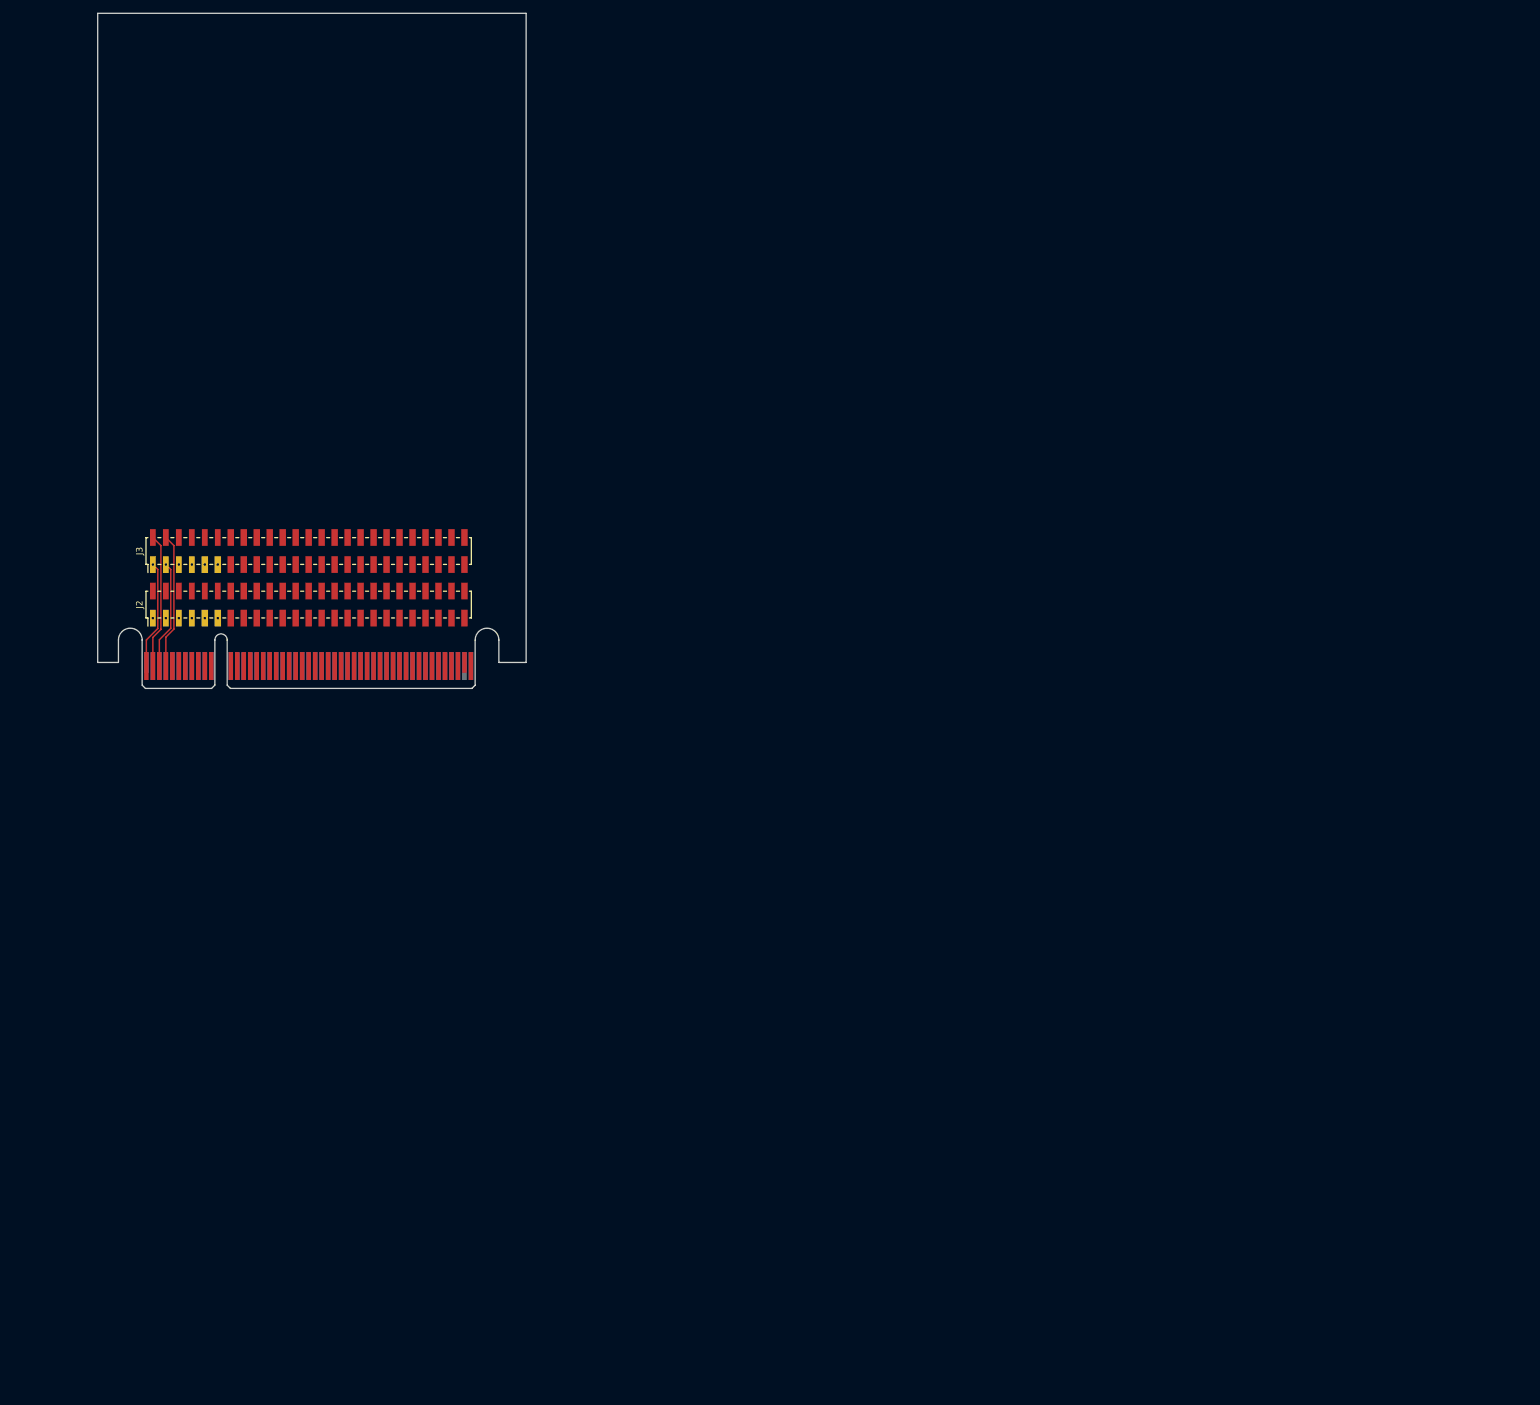
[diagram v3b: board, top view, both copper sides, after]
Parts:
- removed TP1 (x814): TestPoint, proto_board:pad
- J2, J3: footprint Connector_PinHeader_2.00mm:PinHeader_2x25_P2.00mm_Vertical_SMD -> proto_board:PinHeader_2x25_P2.00mm_Vertical_SMD
- moved J2 156.6 mm to (13.5, -12.9)
- moved J3 156.1 mm to (13.5, -21.2)
- moved J1 141.4 mm to (0.00, 0.00)
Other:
- board size 113.1 x 62.3 mm -> 66 x 100 mm
- board text removed: "Conn_02x25_Odd_Even"
